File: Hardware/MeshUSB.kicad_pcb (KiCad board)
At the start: 2 copper layers, 30.4 x 40.8 mm, 33 parts, among them P1 USB_4, P2 PVCell, Q1 MOS_P, U1 XBEE, U2 AP7313-3.3VREGULATOR, U4 FT231X-SSOP, U5 LTC4070

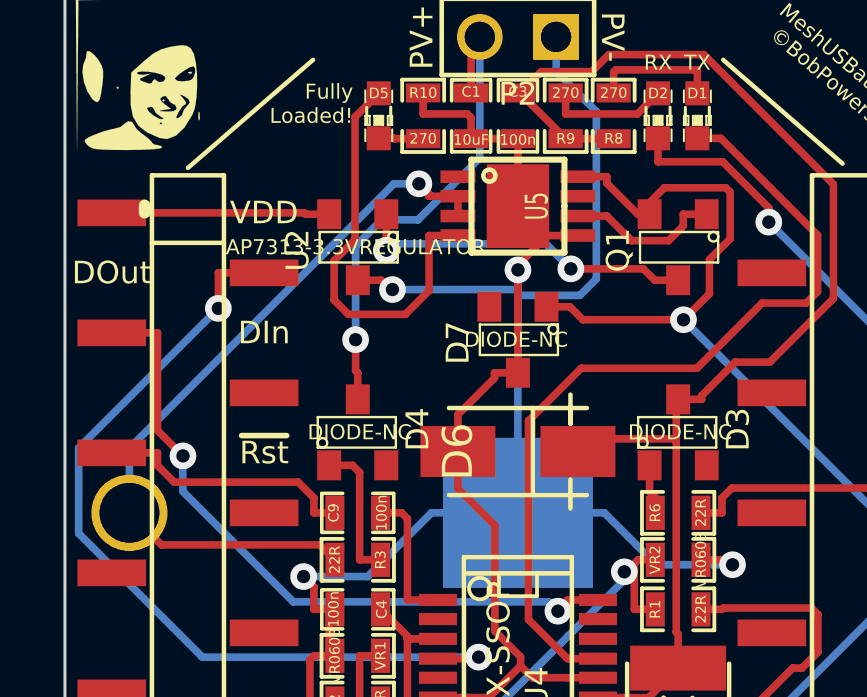
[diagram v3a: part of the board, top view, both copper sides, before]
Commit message: Additional trace to connect everything even in the event the battery holder is not in place.
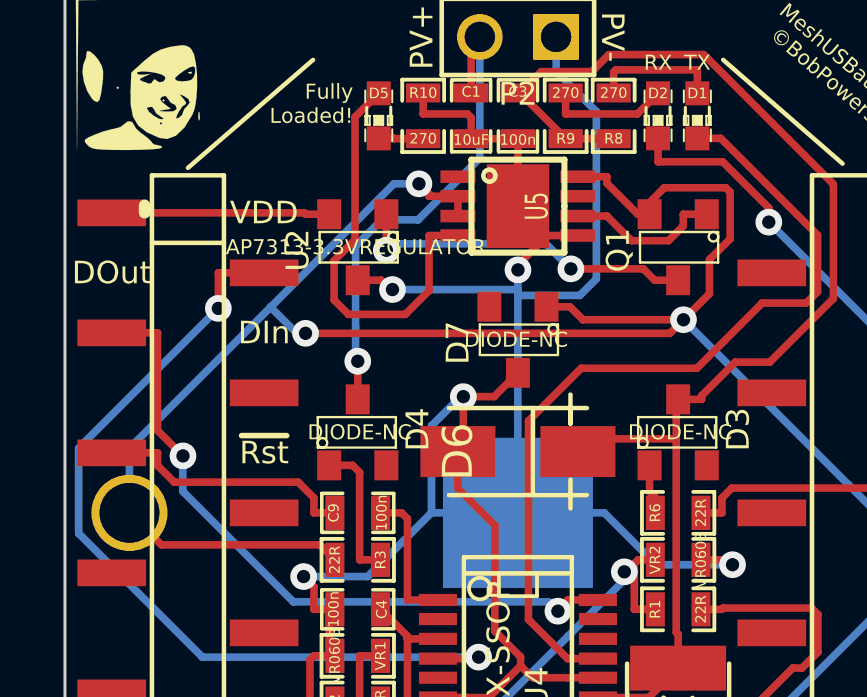
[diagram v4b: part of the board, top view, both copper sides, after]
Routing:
- net N-0000019: track 59.2 -> 73.5 mm, vias 2 -> 3
- net GND: track 95.2 -> 96.2 mm, vias 4 -> 5
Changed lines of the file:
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@@
   (general
     (links 57)
-    (no_connects 1)
-    (area 133.349999 97.699999 163.850001 138.590001)
+    (no_connects 0)
+    (area 130.504334 90.83902 167.053222 140.089)
     (thickness 1.6)
     (drawings 21)
-    (tracks 301)
+    (tracks 313)
     (zones 0)
     (modules 33)
@@
   (segment (start 134.96 105.004) (end 141.3799 105.004) (width 0.254) (layer F.Cu) (net 1))
   (segment (start 142.2075 105.0502) (end 141.4261 105.0502) (width 0.254) (layer F.Cu) (net 1))
+  (segment (start 146.5 112.96) (end 146.68 112.78) (width 0.254) (layer F.Cu) (net 2) (status C00000))
+  (segment (start 146.68 112.78) (end 146.68 111.13) (width 0.254) (layer F.Cu) (net 2) (status 400000))
+  (segment (start 148.5 110.33482) (end 147.70482 111.13) (width 0.254) (layer F.Cu) (net 2) (status 400000))
+  (segment (start 147.70482 111.13) (end 146.68 111.13) (width 0.254) (layer F.Cu) (net 2))
+  (segment (start 146.59 111.13) (end 145.6187 112.1013) (width 0.254) (layer B.Cu) (net 2))
+  (segment (start 145.6187 112.1013) (end 145.6187 115.004) (width 0.254) (layer B.Cu) (net 2))
+  (via (at 146.68 111.13) (size 0.889) (layers F.Cu B.Cu) (net 2))
+  (segment (start 146.68 111.13) (end 146.59 111.13) (width 0.254) (layer B.Cu) (net 2))
+  (segment (start 148.5 115.004) (end 148.5 107.7554) (width 0.254) (layer B.Cu) (net 2))
   (via (at 155.6541 116.7332) (size 0.889) (layers F.Cu B.Cu) (net 2))
   (via (at 148.5 106.9059) (size 0.889) (layers F.Cu B.Cu) (net 2))
   (via (at 141.3552 117.128) (size 0.889) (layers F.Cu B.Cu) (net 2))
+  (segment (start 142.1757 118.22) (end 142.2077 118.22) (width 0.254) (layer F.Cu) (net 2))
+  (segment (start 142.1757 118.22) (end 141.6992 118.22) (width 0.254) (layer F.Cu) (net 2))
+  (segment (start 141.6992 118.22) (end 141.6992 117.472) (width 0.254) (layer F.Cu) (net 2))
+  (segment (start 141.6992 117.472) (end 141.3552 117.128) (width 0.254) (layer F.Cu) (net 2))
+  (segment (start 141.3552 117.128) (end 143.4947 117.128) (width 0.254) (layer B.Cu) (net 2))
+  (segment (start 143.4947 117.128) (end 145.6187 115.004) (width 0.254) (layer B.Cu) (net 2))
   (via (at 144.3171 107.5612) (size 0.889) (layers F.Cu B.Cu) (net 2))
   (segment (start 140.04 123.004) (end 141.5663 123.004) (width 0.254) (layer F.Cu) (net 2))
@@
   (segment (start 148.5 106.9059) (end 148.5 106.7408) (width 0.254) (layer F.Cu) (net 2))
   (segment (start 148.5 115.004) (end 145.6187 115.004) (width 0.254) (layer B.Cu) (net 2))
-  (segment (start 143.4947 117.128) (end 145.6187 115.004) (width 0.254) (layer B.Cu) (net 2))
-  (segment (start 141.3552 117.128) (end 143.4947 117.128) (width 0.254) (layer B.Cu) (net 2))
-  (segment (start 141.6992 117.472) (end 141.3552 117.128) (width 0.254) (layer F.Cu) (net 2))
-  (segment (start 141.6992 118.22) (end 141.6992 117.472) (width 0.254) (layer F.Cu) (net 2))
   (segment (start 151.167 120.4998) (end 150.1507 120.4998) (width 0.254) (layer F.Cu) (net 2))
   (segment (start 145.833 121.1602) (end 146.8493 121.1602) (width 0.254) (layer F.Cu) (net 2))
@@
   (segment (start 141.5664 119.9028) (end 141.6992 119.77) (width 0.254) (layer F.Cu) (net 2))
   (segment (start 141.5664 123.004) (end 141.5664 119.9028) (width 0.254) (layer F.Cu) (net 2))
-  (segment (start 142.1757 118.22) (end 141.6992 118.22) (width 0.254) (layer F.Cu) (net 2))
-  (segment (start 142.1757 118.22) (end 142.2077 118.22) (width 0.254) (layer F.Cu) (net 2))
   (segment (start 142.398 118.22) (end 142.2077 118.22) (width 0.254) (layer F.Cu) (net 2))
   (segment (start 142.2077 118.22) (end 142.2077 119.77) (width 0.254) (layer F.Cu) (net 2))
   (segment (start 142.398 119.77) (end 142.2077 119.77) (width 0.254) (layer F.Cu) (net 2))
   (segment (start 142.2077 119.77) (end 141.6992 119.77) (width 0.254) (layer F.Cu) (net 2))
-  (segment (start 148.5 115.004) (end 148.5 107.7554) (width 0.254) (layer B.Cu) (net 2))
   (segment (start 145.001 127.2604) (end 145.001 129.5087) (width 0.254) (layer F.Cu) (net 2))
   (segment (start 141.5664 123.8258) (end 145.001 127.2604) (width 0.254) (layer F.Cu) (net 2))
@@
   (segment (start 145.34 101.008) (end 145.34 101.7068) (width 0.254) (layer F.Cu) (net 2))
   (segment (start 146.94 102.532) (end 146.94 101.8332) (width 0.254) (layer F.Cu) (net 2))
-  (segment (start 148.5 110.3348) (end 148.5 106.9059) (width 0.254) (layer F.Cu) (net 2))
-  (segment (start 147.7186 110.5101) (end 146.5 111.7287) (width 0.254) (layer F.Cu) (net 2))
-  (segment (start 147.7186 110.3348) (end 147.7186 110.5101) (width 0.254) (layer F.Cu) (net 2))
-  (segment (start 148.5 110.3348) (end 147.7186 110.3348) (width 0.254) (layer F.Cu) (net 2))
-  (segment (start 146.5 112.96) (end 146.5 111.7287) (width 0.254) (layer F.Cu) (net 2))
   (segment (start 147.5305 121.1602) (end 146.8493 121.1602) (width 0.254) (layer F.Cu) (net 2))
   (segment (start 148.5876 120.1031) (end 147.5305 121.1602) (width 0.254) (layer F.Cu) (net 2))
@@
   (segment (start 150.2635 106.8707) (end 149.4296 106.0368) (width 0.254) (layer B.Cu) (net 8))
   (segment (start 144.1125 105.9319) (end 144.1125 106.2512) (width 0.254) (layer F.Cu) (net 8))
-  (via (at 143.088 109.2312) (size 0.889) (layers F.Cu B.Cu) (net 9))
-  (segment (start 146.94 101.008) (end 146.94 100.4363) (width 0.254) (layer F.Cu) (net 9))
-  (segment (start 146.94 99.43) (end 147.23 99.14) (width 0.254) (layer F.Cu) (net 9))
-  (segment (start 146.94 100.4363) (end 146.94 99.43) (width 0.254) (layer F.Cu) (net 9))
-  (segment (start 143.088 110.2665) (end 143.088 109.2312) (width 0.254) (layer F.Cu) (net 9))
-  (segment (start 143.16 110.3385) (end 143.088 110.2665) (width 0.254) (layer F.Cu) (net 9))
+  (segment (start 143.16 111.22018) (end 143.16 109.95) (width 0.254) (layer F.Cu) (net 9))
+  (segment (start 143.088 109.878) (end 143.088 108.828) (width 0.254) (layer B.Cu) (net 9))
+  (segment (start 143.16 109.95) (end 143.088 109.878) (width 0.254) (layer B.Cu) (net 9))
+  (via (at 143.16 109.95) (size 0.889) (layers F.Cu B.Cu) (net 9))
+  (segment (start 143.09 107.46) (end 143.088 107.46) (width 0.254) (layer B.Cu) (net 9))
+  (segment (start 143.088 107.462) (end 143.09 107.46) (width 0.254) (layer B.Cu) (net 9))
+  (segment (start 143.088 108.828) (end 143.088 107.462) (width 0.254) (layer B.Cu) (net 9))
   (segment (start 147.23 103.1798) (end 147.23 99.14) (width 0.254) (layer B.Cu) (net 9))
   (segment (start 145.1701 105.2397) (end 147.23 103.1798) (width 0.254) (layer B.Cu) (net 9))
   (segment (start 143.9561 105.2397) (end 145.1701 105.2397) (width 0.254) (layer B.Cu) (net 9))
   (segment (start 143.088 106.1078) (end 143.9561 105.2397) (width 0.254) (layer B.Cu) (net 9))
-  (segment (start 143.088 109.2312) (end 143.088 106.1078) (width 0.254) (layer B.Cu) (net 9))
-  (segment (start 143.16 111.2202) (end 143.16 110.3385) (width 0.254) (layer F.Cu) (net 9))
+  (segment (start 143.088 107.46) (end 143.088 106.1078) (width 0.254) (layer B.Cu) (net 9))
+  (segment (start 146.94 101.008) (end 146.94 100.4363) (width 0.254) (layer F.Cu) (net 9))
+  (segment (start 146.94 99.43) (end 147.23 99.14) (width 0.254) (layer F.Cu) (net 9))
+  (segment (start 146.94 100.4363) (end 146.94 99.43) (width 0.254) (layer F.Cu) (net 9))
+  (segment (start 154.0178 108.5676) (end 153.5654 109.02) (width 0.254) (layer F.Cu) (net 10))
+  (segment (start 141.13 109.02) (end 140.25425 108.14425) (width 0.254) (layer B.Cu) (net 10))
+  (segment (start 141.42 109.02) (end 141.13 109.02) (width 0.254) (layer B.Cu) (net 10))
+  (via (at 141.42 109.02) (size 0.889) (layers F.Cu B.Cu) (net 10))
+  (segment (start 153.5654 109.02) (end 141.42 109.02) (width 0.254) (layer F.Cu) (net 10))
   (via (at 145.1992 104.0359) (size 0.889) (layers F.Cu B.Cu) (net 10))
+  (segment (start 145.1992 104.0359) (end 144.3626 104.0359) (width 0.254) (layer B.Cu) (net 10))
+  (segment (start 144.3626 104.0359) (end 140.25425 108.14425) (width 0.254) (layer B.Cu) (net 10))
+  (segment (start 146.501 104.4498) (end 145.5355 104.4498) (width 0.254) (layer F.Cu) (net 10))
+  (segment (start 145.5355 104.4498) (end 145.5355 104.3722) (width 0.254) (layer F.Cu) (net 10))
+  (segment (start 145.5355 104.3722) (end 145.1992 104.0359) (width 0.254) (layer F.Cu) (net 10))
+  (segment (start 146.501 105.1102) (end 146.501 104.4498) (width 0.254) (layer F.Cu) (net 10))
   (via (at 154.0178 108.5676) (size 0.889) (layers F.Cu B.Cu) (net 10))
   (segment (start 149.4525 108.1352) (end 150.2338 108.1352) (width 0.254) (layer F.Cu) (net 10))
-  (segment (start 146.501 105.1102) (end 146.501 104.4498) (width 0.254) (layer F.Cu) (net 10))
-  (segment (start 145.5355 104.3722) (end 145.1992 104.0359) (width 0.254) (layer F.Cu) (net 10))
-  (segment (start 145.5355 104.4498) (end 145.5355 104.3722) (width 0.254) (layer F.Cu) (net 10))
-  (segment (start 146.501 104.4498) (end 145.5355 104.4498) (width 0.254) (layer F.Cu) (net 10))
   (segment (start 152.8875 105.0502) (end 152.4968 105.0502) (width 0.254) (layer F.Cu) (net 10))
   (segment (start 136.6174 116.0714) (end 135.55 115.004) (width 0.254) (layer F.Cu) (net 10))
@@
   (segment (start 161.45 115.004) (end 160.4542 115.004) (width 0.254) (layer B.Cu) (net 10))
   (segment (start 135.55 112.8485) (end 135.55 115.004) (width 0.254) (layer B.Cu) (net 10))
-  (segment (start 144.3626 104.0359) (end 135.55 112.8485) (width 0.254) (layer B.Cu) (net 10))
-  (segment (start 145.1992 104.0359) (end 144.3626 104.0359) (width 0.254) (layer B.Cu) (net 10))
+  (segment (start 140.25425 108.14425) (end 135.55 112.8485) (width 0.254) (layer B.Cu) (net 10))
   (segment (start 159.5076 114.0574) (end 154.0178 108.5676) (width 0.254) (layer B.Cu) (net 10))
   (via (at 137.3342 113.106) (size 0.889) (layers F.Cu B.Cu) (net 11))

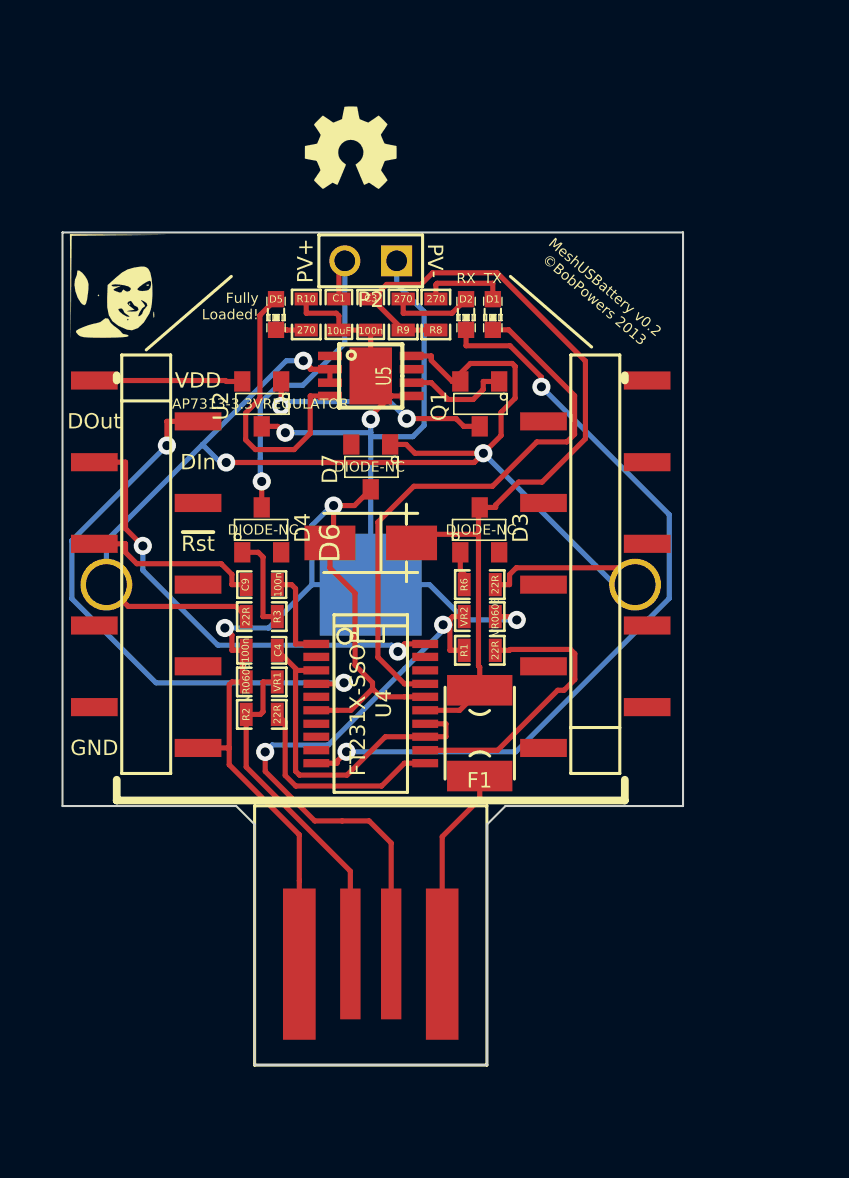
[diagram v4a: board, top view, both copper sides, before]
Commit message: Fixed minor pad spacing error on FT231X non-standard SSOP20 package.
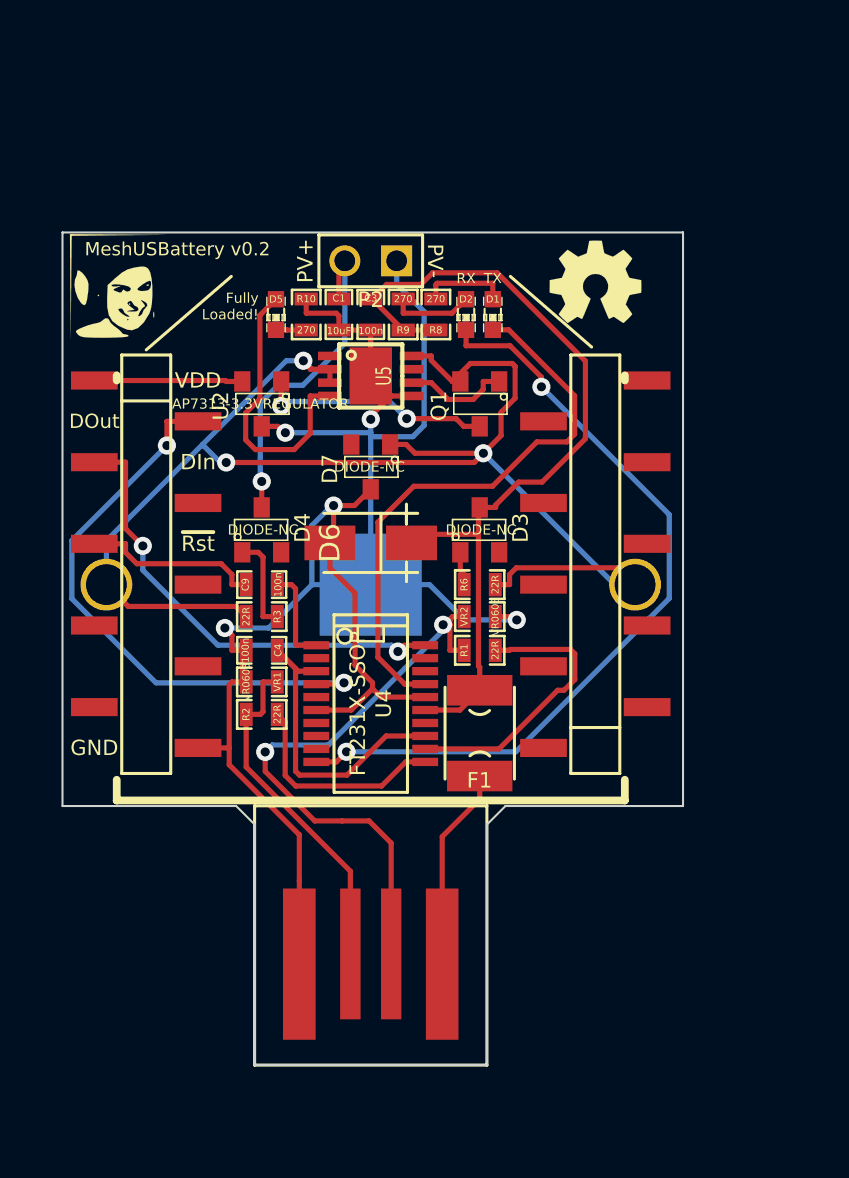
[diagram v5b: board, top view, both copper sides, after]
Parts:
- U4: footprint _MUSB_SSOP20 -> _MUSB_SSOP20-FT231X
- moved G1 13.7 mm to (159.5, 100.2)
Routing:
- net VCCIO: track 17.2 -> 15.9 mm
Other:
- board text added: "MeshUSBattery v0.2"
- board text added: "©BobPowers 2013 OpenHardware Under TAPR OHL tapr.org/OHL"
- board text removed: "MeshUSBattery v0.2 ©BobPowers 2013"

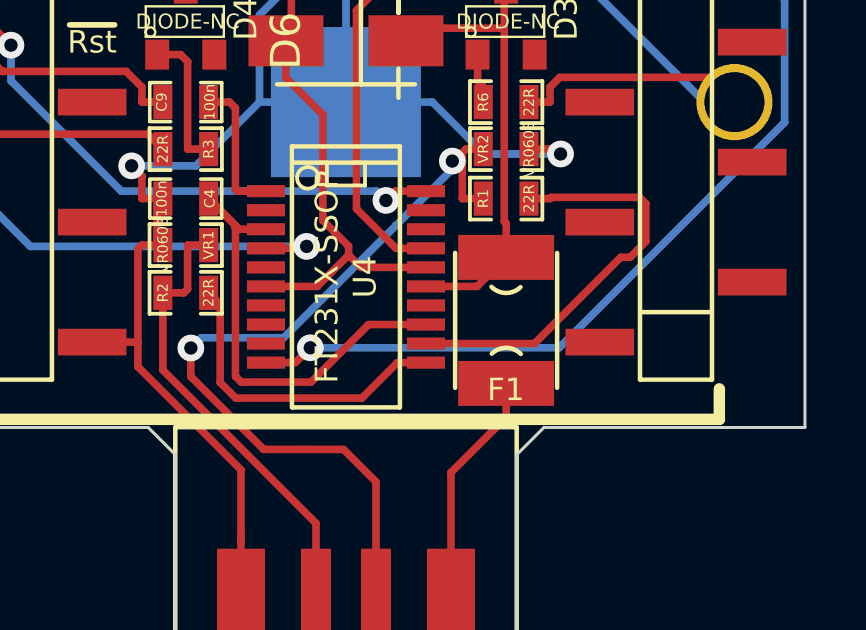
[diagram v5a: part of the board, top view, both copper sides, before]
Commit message: It is probably best to not leave that pin unconnected.
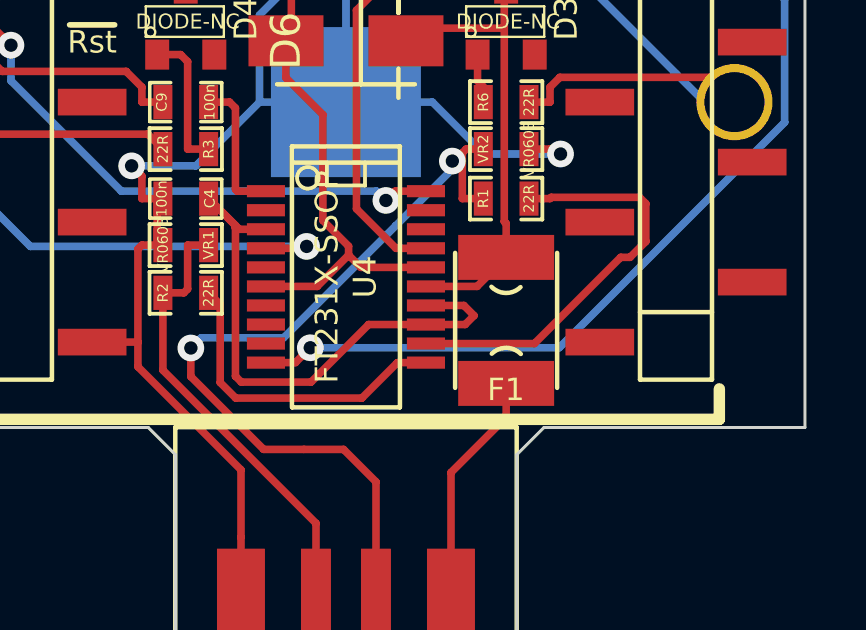
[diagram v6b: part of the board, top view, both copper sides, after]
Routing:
- net VCCIO: track 15.9 -> 19.3 mm
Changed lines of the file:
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@@
   (general
     (links 57)
-    (no_connects 1)
+    (no_connects 0)
     (area 130.504334 90.83902 167.053222 140.089)
     (thickness 1.6)
     (drawings 22)
-    (tracks 306)
+    (tracks 310)
     (zones 0)
     (modules 33)
@@
   (segment (start 150.09 102.532) (end 148.566 101.008) (width 0.254) (layer F.Cu) (net 51))
   (segment (start 148.566 101.008) (end 148.5 101.008) (width 0.254) (layer F.Cu) (net 51))
+  (segment (start 151.167 121.7825) (end 152.4325 121.7825) (width 0.254) (layer F.Cu) (net 52) (status 400000))
+  (segment (start 152.4325 121.7825) (end 152.77 122.12) (width 0.254) (layer F.Cu) (net 52))
+  (segment (start 151.167 122.4175) (end 152.4725 122.4175) (width 0.254) (layer F.Cu) (net 52))
+  (segment (start 152.4725 122.4175) (end 152.77 122.12) (width 0.254) (layer F.Cu) (net 52))
   (segment (start 145.833 119.2425) (end 144.9445 119.2425) (width 0.254) (layer F.Cu) (net 52))
   (segment (start 144.9445 119.2425) (end 143.922 118.22) (width 0.254) (layer F.Cu) (net 52))
